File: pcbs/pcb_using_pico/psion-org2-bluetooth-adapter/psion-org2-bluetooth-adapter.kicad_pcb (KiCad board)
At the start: 2 copper layers, 129.7 x 100 mm, 54 parts, among them J1 Conn_02x08_Odd_Even, J2 Conn_01x03_Female, J3 Barrel_Jack, J5 Conn_01x04_Female, J7 Conn_01x03_Female, M1 P-CHANNEL-MOSFET, U1 74LS245, U2 74LS245, U3 Pico, U4 ESP32-WROOM-32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

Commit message: Changed circuit to new power arrangement
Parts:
- removed C12, C13, C14: 100nF, Capacitor_SMD:C_0805_2012Metric
- removed U6: AMS1117-3.3, Package_TO_SOT_SMD:SOT-223-3_TabPin2
- added C9: 100nF, Capacitor_SMD:C_0805_2012Metric, F.Cu at (161.5, 78.2)
- added D4: D_Schottky, Diode_SMD:D_SOD-123, F.Cu at (172.3, 74.2)
- R1, R2: value R_Small -> 10k
- R6: value R_Small -> 47k
- U5: value BQ24072RGT -> BQ24079RGT
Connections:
- C11 pad 1: VREG -> Net-(C11-Pad1)
- C5 pad 1: VIN -> Net-(C5-Pad1)
- C6 pad 1: VIN -> Net-(C5-Pad1)
- J3 pad 1: VIN -> Net-(C11-Pad1)
- U5 pad 13: VIN -> Net-(C5-Pad1)
- U7 pad 2: +5V -> Net-(C5-Pad1)
- U7 pad 3: VREG -> Net-(D4-Pad1)
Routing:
- net Net-(C5-Pad1): track 0.00 -> 114.5 mm, vias 0 -> 4
- net VIN: track 104.4 -> 0.00 mm, vias 2 -> 0
- net Net-(C11-Pad1): track 0.00 -> 60.0 mm, vias 0 -> 2
- net +5V: track 19.8 -> 0.00 mm, vias 2 -> 0
- net +3V3: track 188.7 -> 169.3 mm
- net VREG: track 114.1 -> 99.5 mm, vias 5 -> 4
- net Net-(D4-Pad1): track 0.00 -> 6.13 mm
- net GND: track 699.0 -> 701.9 mm
- net Net-(R12-Pad2): track 17.0 -> 14.6 mm

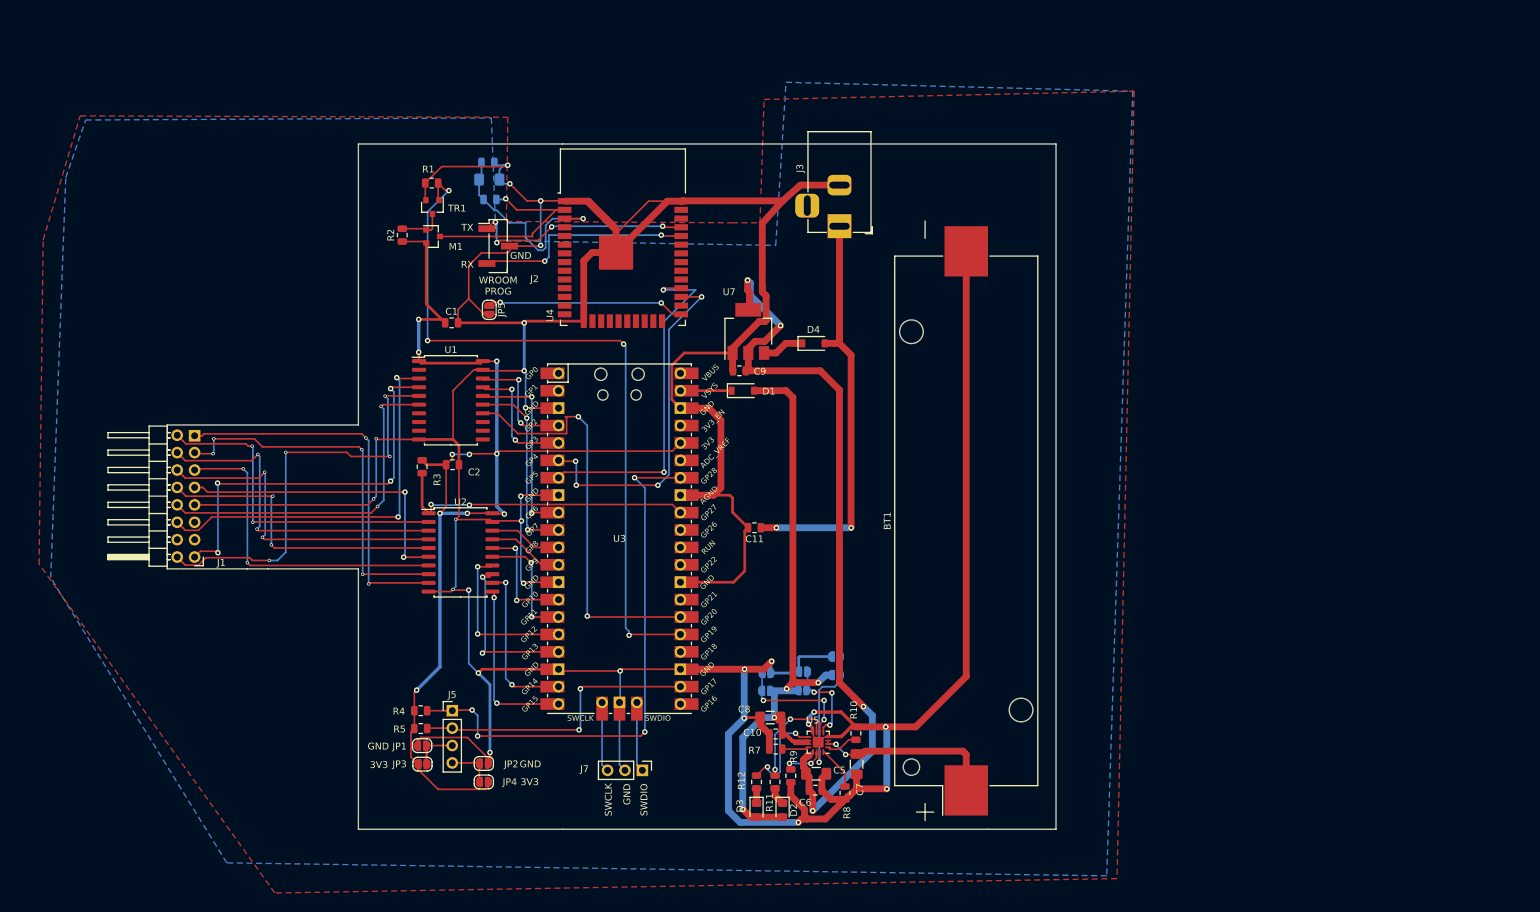
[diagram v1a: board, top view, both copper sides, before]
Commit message: Merged erroneous changes to V1.0 archive started
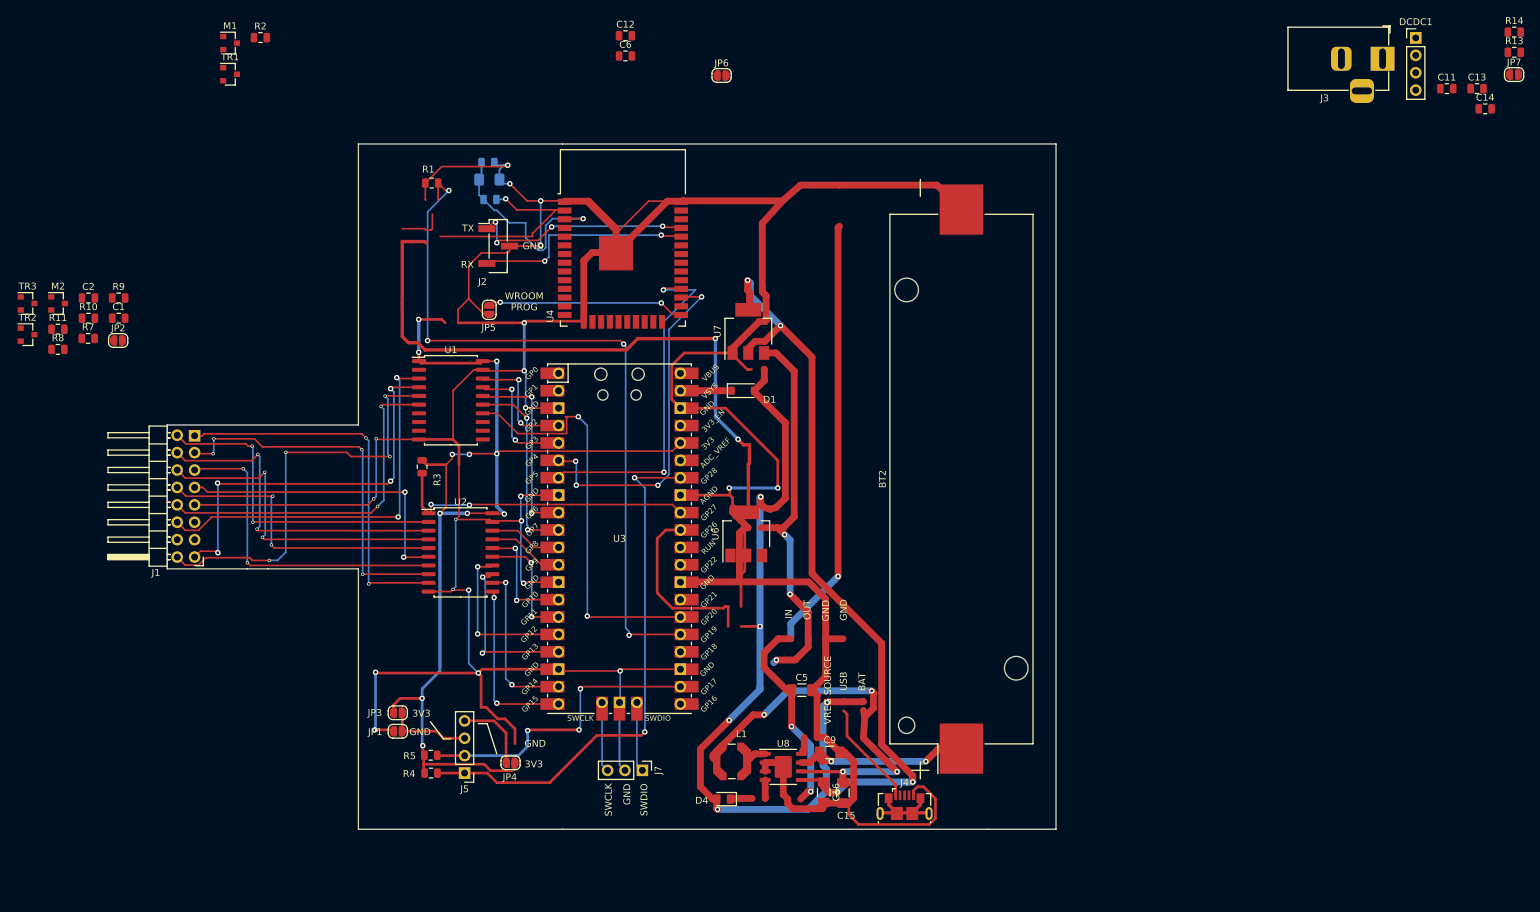
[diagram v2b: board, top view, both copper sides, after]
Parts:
- removed BT1: Battery_Cell, Battery:BatteryHolder_Keystone_1042_1x18650
- removed C10: 100nF, Capacitor_SMD:C_0805_2012Metric
- removed C7: 4u7, Capacitor_SMD:C_1206_3216Metric_Pad1.42x1.75mm_HandSolder
- removed C8: 10uF, Capacitor_SMD:C_1206_3216Metric_Pad1.42x1.75mm_HandSolder
- removed D2, D3: LED, LED_SMD:LED_0805_2012Metric_Pad1.15x1.40mm_HandSolder
- removed JP10, JP11, JP8, JP9: Jumper_NO_Small, Jumper:SolderJumper-2_P1.3mm_Open_RoundedPad1.0x1.5mm
- removed R12: R_Small, Resistor_SMD:R_0805_2012Metric
- removed U5: BQ24079RGT, Package_DFN_QFN:VQFN-16-1EP_3x3mm_P0.5mm_EP1.6x1.6mm
- added BT2: Battery_Cell, Battery:BatteryHolder_Keystone_1042_1x18650, F.Cu at (193.9, 94.0)
- added C12: 100nF, Capacitor_SMD:C_0805_2012Metric, F.Cu at (144.9, 29.3)
- added C13: 100nF, Capacitor_SMD:C_0805_2012Metric, F.Cu at (269.1, 37.0)
- added C14: 100nF, Capacitor_SMD:C_0805_2012Metric, F.Cu at (270.3, 40.0)
- added C15: 22uF, Capacitor_SMD:C_1206_3216Metric_Pad1.42x1.75mm_HandSolder, F.Cu at (176.6, 139.8)
- added C16: 10uF, Capacitor_SMD:C_1206_3216Metric_Pad1.42x1.75mm_HandSolder, F.Cu at (173.8, 139.7)
- added DCDC1: dcdc, Connector_PinHeader_2.54mm:PinHeader_1x04_P2.54mm_Vertical, F.Cu at (260.2, 29.6)
- added J4: Connector_USB_B_Micro, Connector_USB:USB_Micro-B_GCT_USB3076-30-A, F.Cu at (185.6, 141.6)
- added L1: 2.2uH, Inductor_SMD:L_Coilcraft_LPS5030, F.Cu at (160.4, 135.2)
- added M2: Si2301, Package_TO_SOT_SMD:SOT-23, F.Cu at (62.1, 68.4)
- added R13: 2k2, Resistor_SMD:R_0805_2012Metric, F.Cu at (274.6, 31.7)
- added R14: 500R, Resistor_SMD:R_0805_2012Metric, F.Cu at (274.6, 28.8)
- added TR2: si2302, Package_TO_SOT_SMD:SOT-23, F.Cu at (57.6, 72.9)
- added TR3: Si2302, Package_TO_SOT_SMD:SOT-23, F.Cu at (57.6, 68.4)
- added U6: AMS1117-3.3, Package_TO_SOT_SMD:SOT-223-3_TabPin2, F.Cu at (162.5, 102.0)
- added U8: ETA6002, Package_SO:SOIC-8-1EP_3.9x4.9mm_P1.27mm_EP2.514x3.2mm, F.Cu at (167.9, 136.0)
- C9: value 100nF -> 1uF; footprint Capacitor_SMD:C_0805_2012Metric -> Capacitor_SMD:C_1206_3216Metric_Pad1.42x1.75mm_HandSolder
- D4: value D_Schottky -> LED; footprint Diode_SMD:D_SOD-123 -> LED_SMD:LED_0805_2012Metric_Pad1.15x1.40mm_HandSolder
- JP6, JP7: moved to F.Cu
- R1, R10, R2: value 10k -> R_Small
- R6: value 47k -> R_Small
- moved JP7 139.7 mm to (274.5, 35.0), turned to 0 degrees
- moved R8 131.8 mm to (62.1, 75.1), turned to 0 degrees
- moved R10 127.3 mm to (66.5, 70.5), turned to 0 degrees
- moved R11 123.8 mm to (62.1, 72.1), turned to 0 degrees
- moved R9 120.3 mm to (70.9, 67.6), turned to 0 degrees
- moved C11 119.6 mm to (264.7, 37.0), turned to 0 degrees
- moved R7 116.9 mm to (66.5, 73.5), turned to 0 degrees
- moved C6 110.7 mm to (144.9, 32.3)
- moved JP6 90.0 mm to (158.9, 35.1), turned to 0 degrees
- moved J3 82.9 mm to (255.3, 32.7), turned to 0 degrees
- moved JP2 81.6 mm to (70.8, 73.8)
- moved D4 67.8 mm to (159.2, 140.7), turned to 180 degrees
- moved C2 58.4 mm to (66.5, 67.6)
- moved C9 57.2 mm to (174.7, 133.9), turned to 0 degrees
- moved C1 48.6 mm to (70.9, 70.5)
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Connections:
- C9 pad 1: Net-(C5-Pad1) -> Net-(BT2-Pad1)
- D4 pad 2: Net-(C11-Pad1) -> VREG
- J1 pad 13: (no net) -> VCC
- J3 pad 1: Net-(C11-Pad1) -> Net-(C5-Pad1)
- JP6 pad 2: Net-(JP6-Pad2) -> Net-(C15-Pad1)
- JP7 pad 1: GND -> VREG
- JP7 pad 2: Net-(JP6-Pad2) -> Net-(J4-Pad1)
- M1 pad 2: +3V3 -> ESP_3V3
- R10 pad 1: Net-(R10-Pad1) -> VCC
- R10 pad 2: GND -> Net-(M2-Pad1)
- R11 pad 1: Net-(D2-Pad1) -> TRI_TX
- R11 pad 2: Net-(R11-Pad2) -> GND
- R2 pad 1: +3V3 -> ESP_3V3
- R7 pad 1: Net-(R7-Pad1) -> VREG
- R7 pad 2: GND -> Net-(R7-Pad2)
- R8 pad 1: Net-(R8-Pad1) -> Net-(R7-Pad2)
- R9 pad 2: GND -> SD3
- U3 pad 21: Net-(U3-Pad21) -> TRI_TX
- U3 pad 24: Net-(U3-Pad24) -> TX_TO_PSION
- U3 pad 31: Net-(U3-Pad31) -> Net-(R7-Pad2)
- U7 pad 2: Net-(C5-Pad1) -> Net-(C14-Pad1)
- U7 pad 3: Net-(D4-Pad1) -> Net-(C11-Pad1)
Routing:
- net Net-(C14-Pad1): track 0.00 -> 112.5 mm, vias 0 -> 4
- net ESP_3V3: track 0.00 -> 91.9 mm, vias 0 -> 2
- net Net-(C15-Pad1): track 0.00 -> 59.2 mm, vias 0 -> 4
- net GND: track 701.9 -> 653.0 mm, vias 26 -> 21
- net VREG: track 99.5 -> 137.5 mm, vias 4 -> 5
- net Net-(BT2-Pad1): track 0.00 -> 28.0 mm, vias 0 -> 2
- net Net-(BT1-Pad1): track 27.0 -> 0.00 mm, vias 2 -> 0
- net Net-(R7-Pad2): track 0.00 -> 26.1 mm
- net Net-(C5-Pad1): track 114.5 -> 93.3 mm, vias 4 -> 3
- net Net-(JP10-Pad1): track 19.3 -> 0.00 mm, vias 1 -> 0
- net Net-(JP6-Pad2): track 17.9 -> 0.00 mm, vias 3 -> 0
- net Net-(J4-Pad1): track 0.00 -> 15.4 mm
- net Net-(R11-Pad2): track 14.8 -> 0.00 mm, vias 2 -> 0
- net Net-(R12-Pad2): track 14.6 -> 0.00 mm, vias 2 -> 0
- net Net-(JP8-Pad2): track 13.2 -> 0.00 mm, vias 3 -> 0
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- removed copper zone on B.Cu, net +3V3
- removed copper zone on F.Cu, net GND
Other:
- board text added: "BAT"
- board text added: "IN"
- board text added: "OUT"
- board text added: "Psion Organiser II Bluetooth Adapter Feb 2022 menadue@gmail.com V2.0"
- board text added: "USB"
- board text added: "VREG SOURCE"
- board text removed: "EN1"
- board text removed: "EN2"
- board text removed: "Psion Organiser II Bluetooth Adapter Dec 2021 menadue@gmail.com V1.0"
- board text removed: "TD"
- board text removed: "VREG"

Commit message: V2.0 sent off for fab. New charger IC with more solderable footprint, plus other fixes
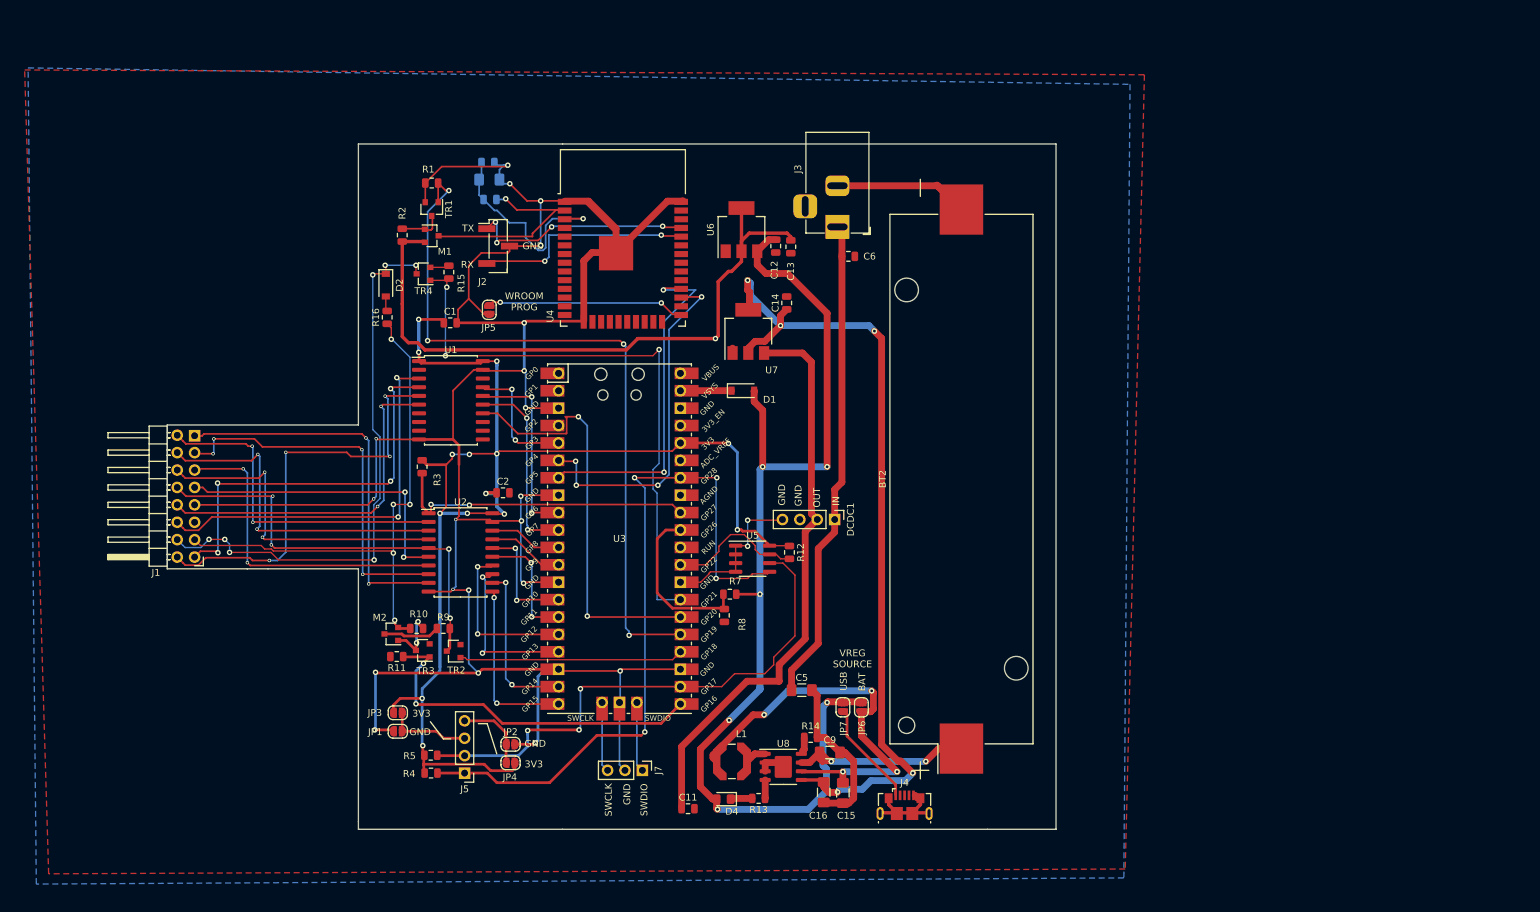
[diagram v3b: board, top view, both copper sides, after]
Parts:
- added D2: D_Schottky, Diode_SMD:D_SOD-123, F.Cu at (109.9, 65.7)
- added R12: R_Small, Resistor_SMD:R_0805_2012Metric, F.Cu at (168.8, 104.7)
- added R15: 47k, Resistor_SMD:R_0805_2012Metric, F.Cu at (119.1, 63.8)
- added R16: 47k, Resistor_SMD:R_0805_2012Metric, F.Cu at (110.1, 70.4)
- added TR4: New_Library_Si2302CDS-n-channel, Package_TO_SOT_SMD:SOT-23, F.Cu at (115.4, 64.0)
- added U5: 24LC32, Package_SO:SOIC-8_3.9x4.9mm_P1.27mm, F.Cu at (163.4, 105.6)
- moved R13 155.0 mm to (164.3, 140.6), turned to 180 degrees
- moved C11 152.6 mm to (154.0, 142.1)
- moved R14 145.4 mm to (171.9, 131.7)
- moved JP7 134.6 mm to (176.6, 127.3), turned to 270 degrees
- moved DCDC1 110.1 mm to (175.4, 99.9), turned to 270 degrees
- moved C14 105.8 mm to (168.4, 68.3), turned to 90 degrees
- moved R8 104.7 mm to (159.3, 113.9), turned to 270 degrees
- moved C13 102.8 mm to (169.0, 60.1), turned to 270 degrees
- moved R7 100.8 mm to (160.1, 110.8), turned to 180 degrees
- moved JP6 94.4 mm to (179.3, 127.3), turned to 270 degrees
- moved J3 83.2 mm to (175.8, 57.2), turned to 270 degrees
- moved JP2 82.2 mm to (128.1, 132.7)
- moved TR2 77.4 mm to (119.8, 119.1), turned to 180 degrees
- moved TR3 76.7 mm to (115.3, 119.0), turned to 180 degrees
- moved R11 68.8 mm to (111.5, 119.9), turned to 180 degrees
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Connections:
- net RUN renamed Net-(U3-Pad30)
- net VBUS renamed Net-(U3-Pad40)
- J1 pad 14: (no net) -> AC
- J4 pad 6: Net-(J4-Pad6) -> GND
- U1 pad 18: P_SPGM -> (no net)
- U3 pad 27: IP_CLK -> AC_ON
- U3 pad 29: OP_CLK -> EEPROM_WP
- U3 pad 4: P_SPGM -> Net-(U3-Pad4)
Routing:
- net GND: track 653.0 -> 474.8 mm, vias 21 -> 22
- net AC_ON: track 0.00 -> 86.3 mm, vias 0 -> 3
- net AC: track 0.00 -> 83.1 mm, vias 0 -> 7
- net VCC: track 0.00 -> 80.1 mm, vias 0 -> 5
- net TRI_TX: track 0.00 -> 52.5 mm, vias 0 -> 2
- net VREG: track 137.5 -> 178.0 mm, vias 5 -> 6
- net I2C_SCLK: track 44.4 -> 78.2 mm
- net TX_TO_PSION: track 0.00 -> 32.7 mm
- net +3V3: track 161.0 -> 192.9 mm, vias 11 -> 14
- net I2C_SDA: track 78.5 -> 106.7 mm, vias 2 -> 4
- net Net-(C11-Pad1): track 57.3 -> 83.9 mm, vias 3 -> 0
- net Net-(C5-Pad1): track 93.3 -> 71.2 mm, vias 3 -> 0
- net EEPROM_WP: track 0.00 -> 20.1 mm
- net SD3: track 44.8 -> 63.0 mm, vias 2 -> 4
- net P_SPGM: track 17.5 -> 0.00 mm, vias 2 -> 0
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- added copper zone on B.Cu, net +3V3
- added copper zone on F.Cu, net GND

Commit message: Updates, psion link not working
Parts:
- R10, R11: value R_Small -> 10k
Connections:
- U8 pad 5: Net-(C14-Pad1) -> Net-(R14-Pad1)
- U8 pad 6: Net-(C15-Pad1) -> Net-(BT2-Pad1)
- U8 pad 7: Net-(BT2-Pad1) -> Net-(C15-Pad1)
- U8 pad 8: Net-(R14-Pad1) -> Net-(C14-Pad1)
